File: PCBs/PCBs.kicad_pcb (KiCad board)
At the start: 2 copper layers, 6 parts, among them U6 TPS62172DSG

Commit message: buck converter
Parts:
- added BuckConverter3-17V->3.3V-ScrewTerminalInput1: Input, TerminalBlock_4Ucon:TerminalBlock_4Ucon_1x02_P3.50mm_Horizontal, F.Cu at (134.7, 94.5)
- added BuckConverter3-17V->3.3V-ScrewTerminalOutput1: Output, TerminalBlock_4Ucon:TerminalBlock_4Ucon_1x02_P3.50mm_Horizontal, F.Cu at (155.4, 98.0)
- moved BuckConverter3-17V->3.3V-C2 9.95 mm to (149.9, 97.9)
- moved BuckConverter3-17V->3.3V-C1 9.36 mm to (140.0, 96.2), turned to -90 degrees
- moved BuckConverter3-17V->3.3V-LED1 0.40 mm to (146.1, 94.8)
- moved BuckConverter3-17V->3.3V-R1 0.40 mm to (148.6, 94.8)
- moved BuckConverter3-17V->3.3V-L1 0.20 mm to (146.1, 96.0)
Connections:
- BuckConverter3-17V->3.3V-C1 pad 1: VCC -> VCCIN
- BuckConverter3-17V->3.3V-C2 pad 2: VCC -> VCCOUT
- BuckConverter3-17V->3.3V-L1 pad 2: VCC -> VCCOUT
- BuckConverter3-17V->3.3V-R1 pad 2: VCC -> VCCOUT
- U6 pad 2: VCC -> VCCIN
- U6 pad 3: VCC -> VCCIN
- U6 pad 6: VCC -> VCCOUT
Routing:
- net VCCOUT: track 0.00 -> 18.6 mm
- net GND: track 0.00 -> 7.40 mm, vias 0 -> 2
- net VCCIN: track 0.00 -> 3.97 mm, vias 0 -> 1
- net Net-(BuckConverter3-17V->3.3V-LED1-K): track 0.00 -> 1.71 mm
- net Net-(BuckConverter3-17V->3.3V-LED1-A): track 0.00 -> 1.49 mm
- net Net-(U6-SW): track 0.00 -> 1.46 mm
- added copper zone on In1.Cu, net GND
- added copper zone on In2.Cu, net VCCIN
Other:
- board outline added: 29.8 x 11.3 mm
- copper layers 2 -> 4
- board text added: "+"
- board text added: "-"
- board text added: "Buck Converter V1.00 Input 3-17V -> Fixed 3.3V 500mA"
- board text added: "C1"
- board text added: "C2"
- board text added: "Input"
- board text added: "L1"
- board text added: "Output"
- board text added: "R1"
- board text added: "TPS62172DSGR"

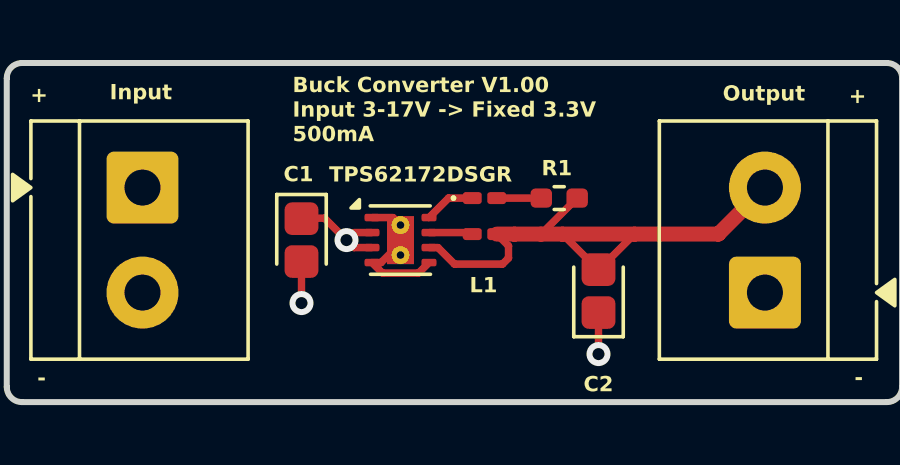
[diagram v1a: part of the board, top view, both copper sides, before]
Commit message: vias under pads and other changes
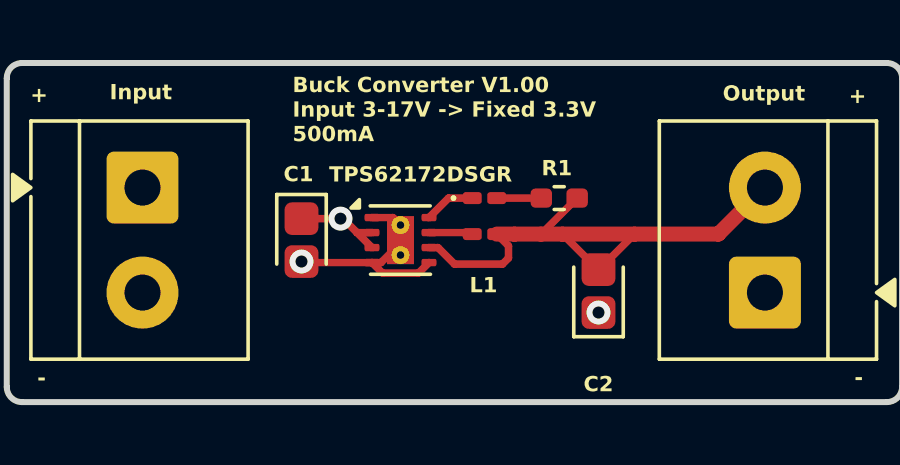
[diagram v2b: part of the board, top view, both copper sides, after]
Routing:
- net VCCIN: track 3.97 -> 3.46 mm
